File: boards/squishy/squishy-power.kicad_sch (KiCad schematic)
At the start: 48 parts, among them SW1 RST, U1 LFE5UM5G-45F-8BG381C, U10 TPS720115QDRVRQ1, U2 W25N01GVZEIG, U5 APX811-40UG-7, U7 TPS73733DRVR, U8 TPS7A1125PDRVT, U9 TPS7A1118PDRVT

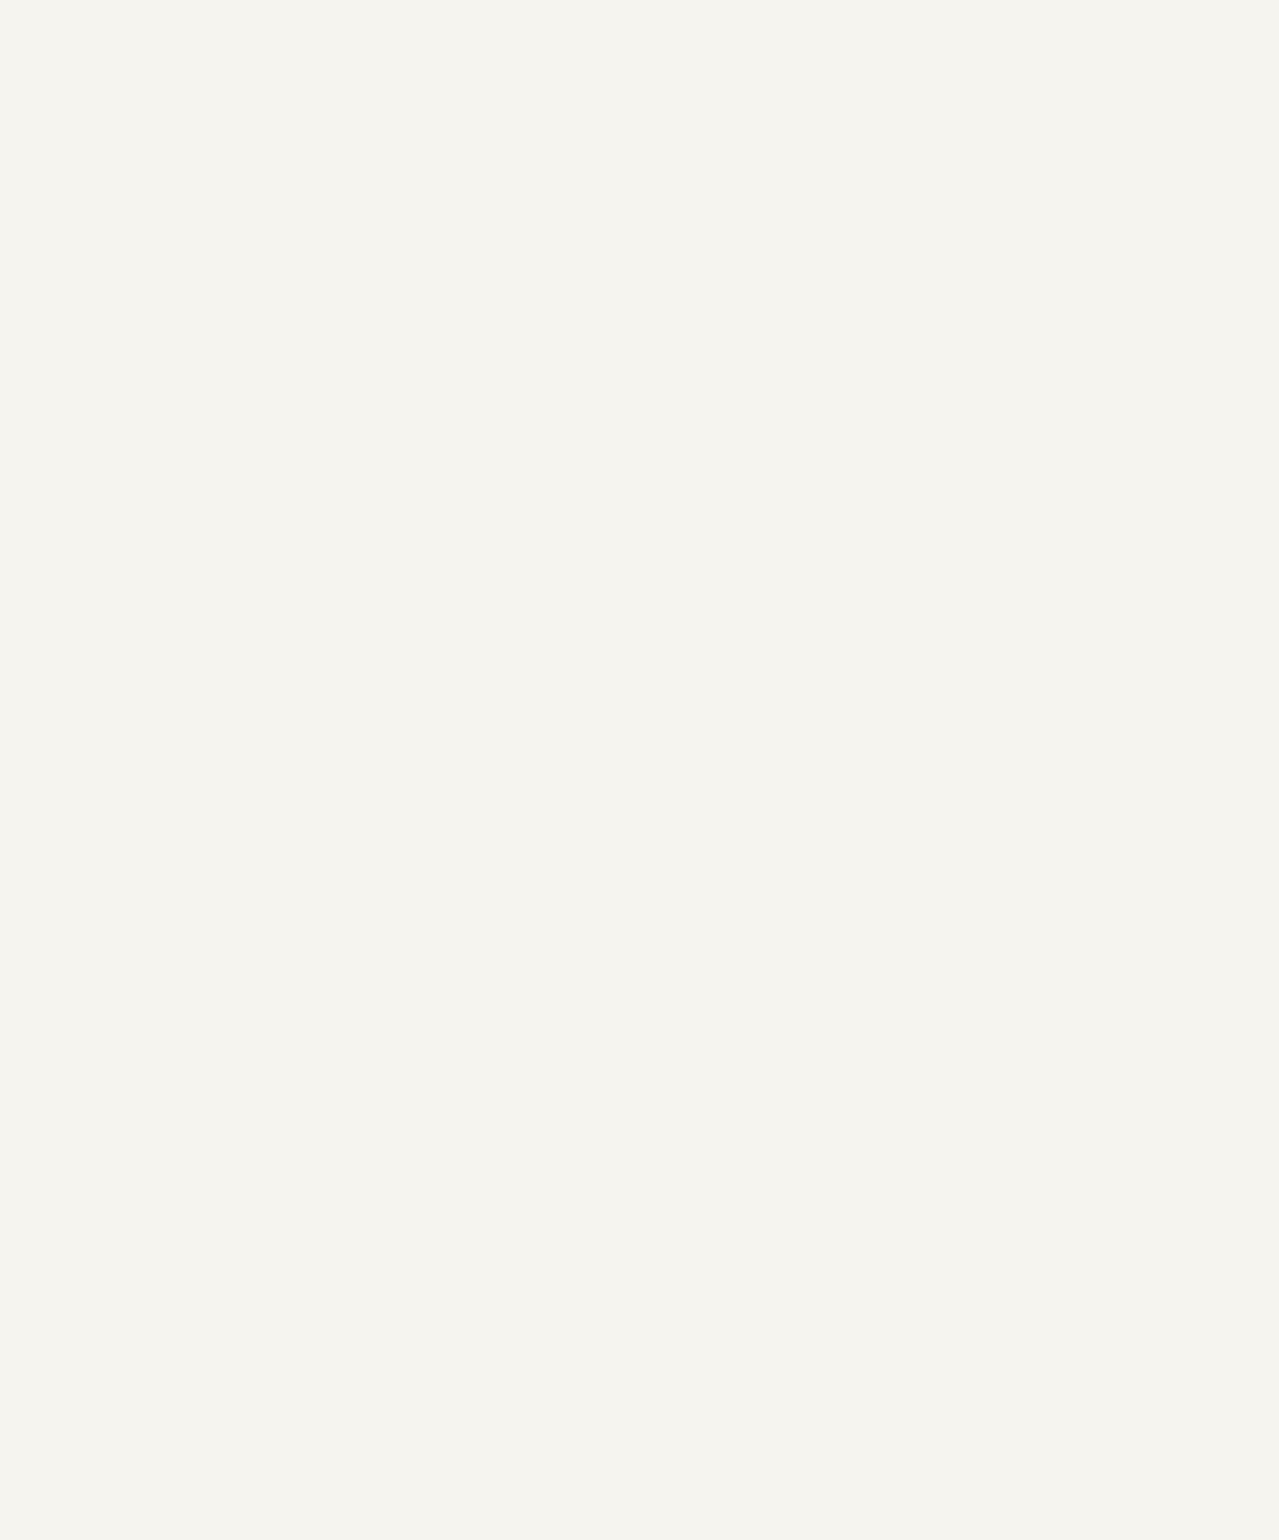
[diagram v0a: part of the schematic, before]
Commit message: hardware: large amount of refactoring and schematic tetris, slowly getting everything hooked back up, also merrged all the DFU/Debug signals onto a single connector
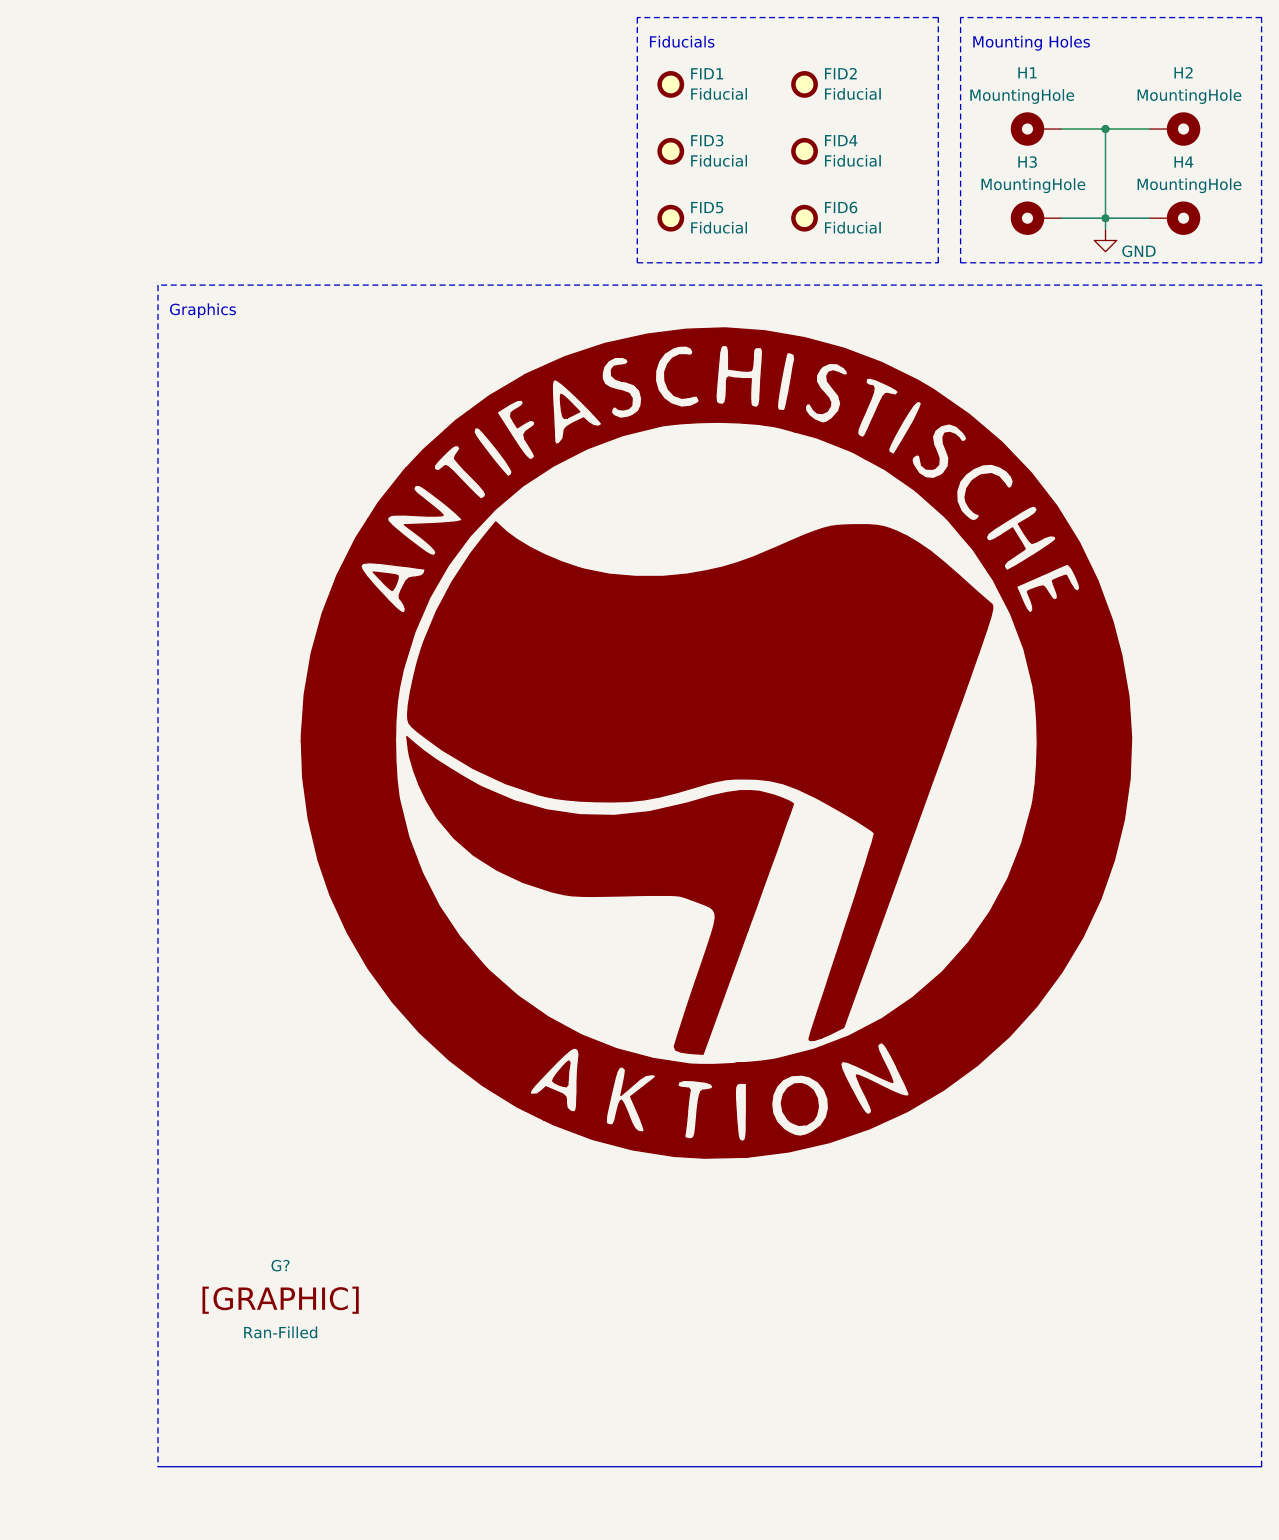
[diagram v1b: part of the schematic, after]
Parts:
- added FID1, FID2, FID3, FID4, FID5, FID6: Fiducial, Fiducial:Fiducial_0.75mm_Mask1.5mm, symbol Mechanical:Fiducial
- added G?: Ran-Filled, lethalbit-graphics:yuki_10x11, symbol lethalbit-graphics:Graphic
- added G?: Antifaschistische_Aktion, DX-MON:Antifaschistische-Aktion_Inv_600dpi, symbol lethalbit-graphics:Antifaschistische_Aktion
- added H1, H2, H3, H4: MountingHole, MountingHole:MountingHole_3.2mm_M3_Pad, symbol Mechanical:MountingHole_Pad
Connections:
- net GND: now also H1.1, H2.1, H3.1, H4.1
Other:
- note added: "Fiducials"
- note added: "Graphics"
- note added: "Mounting Holes"

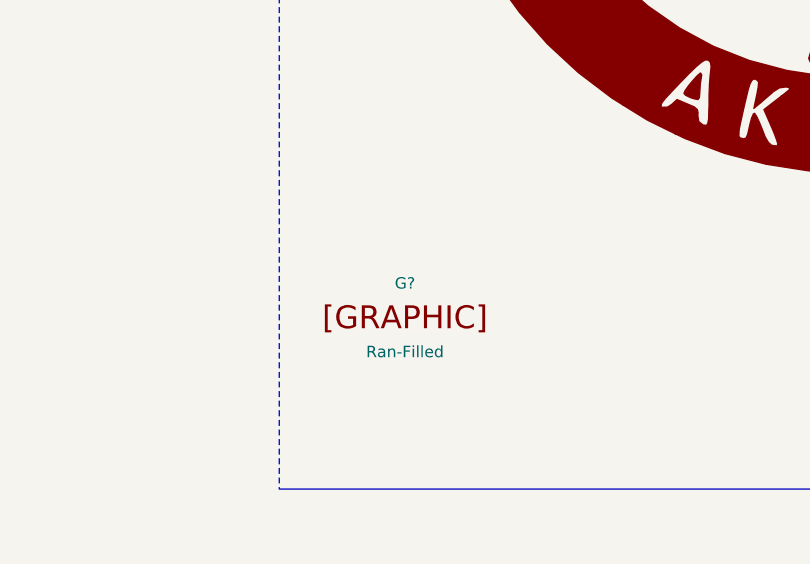
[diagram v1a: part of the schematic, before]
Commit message: hardware: some more refactoring, prior to a full PCB rip-up and re-layout
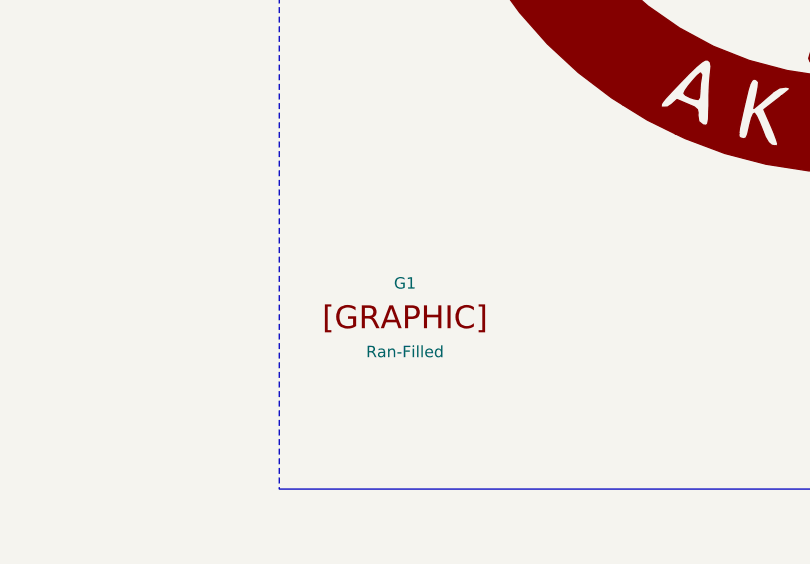
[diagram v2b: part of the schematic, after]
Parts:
- gave numbers to parts that had none: 2
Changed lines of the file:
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@@
   (symbol (lib_id "power:GND") (at 388.62 38.1 0) (unit 1)
     (in_bom yes) (on_board yes)
-    (property "Reference" "#PWR?" (id 0) (at 388.62 44.45 0)
+    (property "Reference" "#PWR0110" (id 0) (at 388.62 44.45 0)
       (effects (font (size 1.27 1.27)) hide)
     )
@@
   (symbol (lib_id "lethalbit-graphics:Graphic") (at 294.64 160.02 0) (unit 1)
     (in_bom no) (on_board yes)
-    (property "Reference" "G?" (id 0) (at 294.64 156.21 0))
+    (property "Reference" "G1" (id 0) (at 294.64 156.21 0))
     (property "Value" "Ran-Filled" (id 1) (at 294.64 163.83 0))
     (property "Footprint" "lethalbit-graphics:yuki_10x11" (id 2) (at 294.64 160.02 0)
@@
   (symbol (lib_id "lethalbit-graphics:Antifaschistische_Aktion") (at 344.17 46.99 0) (unit 1)
     (in_bom no) (on_board yes)
-    (property "Reference" "G?" (id 0) (at 392.2522 95.4532 0)
+    (property "Reference" "G2" (id 0) (at 392.2522 95.4532 0)
       (effects (font (size 1.27 1.27)) (justify left) hide)
     )

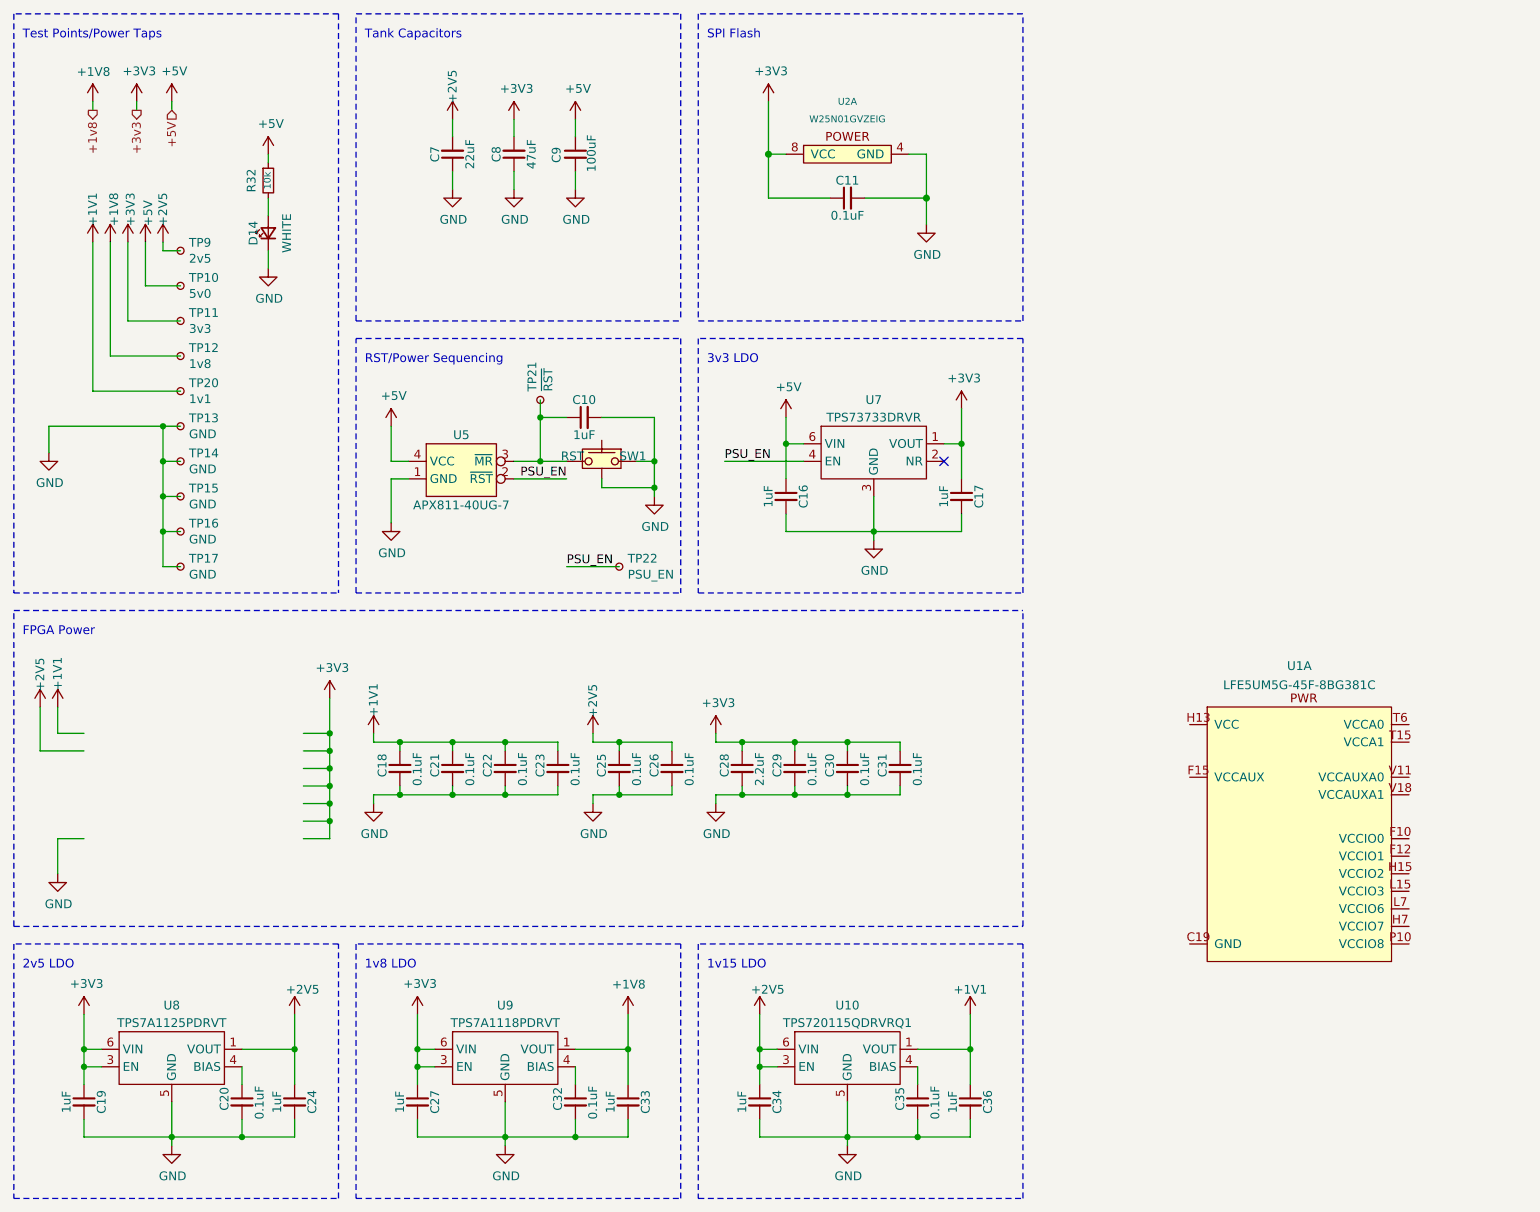
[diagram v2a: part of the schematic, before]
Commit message: hardware: added back the 1v8 regulated as we need the ULPI PHY again for USB2 compatibility, also updated the sheet metadata
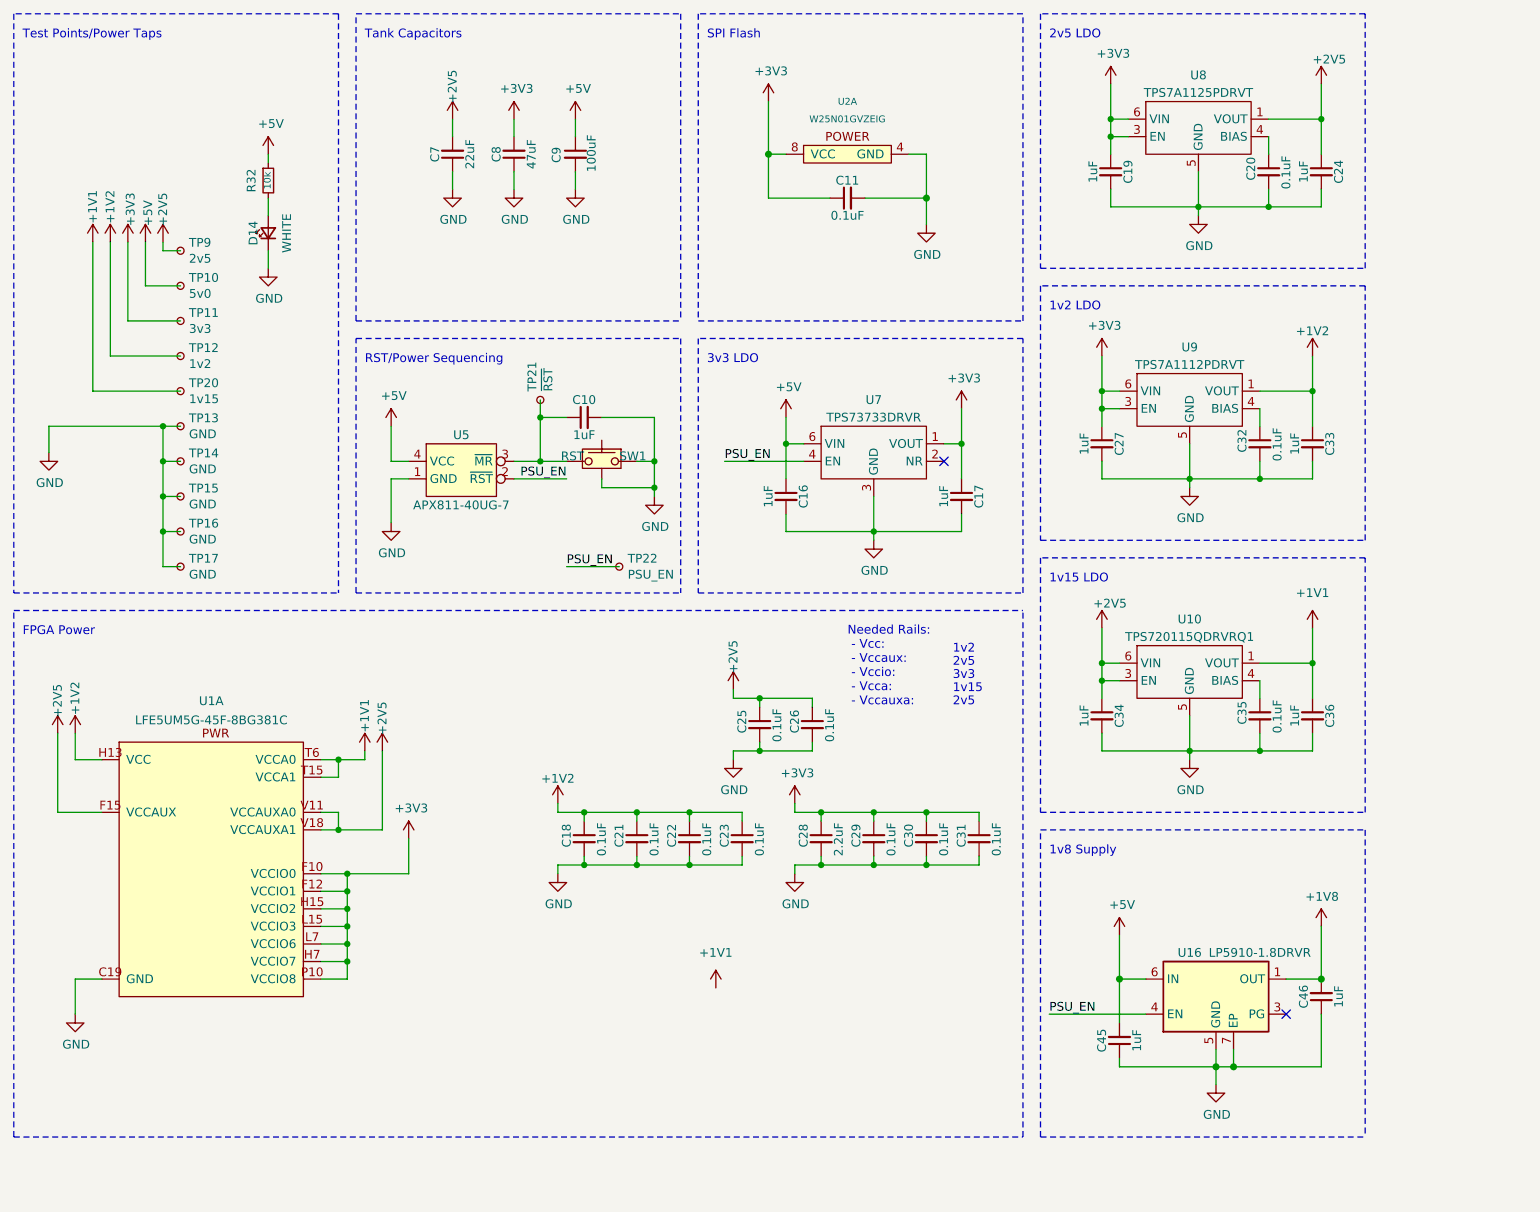
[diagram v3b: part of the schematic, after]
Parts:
- added C45, C46: 1uF, Capacitor_SMD:C_0603_1608Metric, symbol Device:C_Small
- added U16: LP5910-1.8DRVR, Package_SON:WSON-6-1EP_2x2mm_P0.65mm_EP1x1.6mm_ThermalVias, symbol Regulator_Linear:LP5912-1.8DRV
- TP12: value 1v8 -> 1v2
- TP20: value 1v1 -> 1v15
- U9: value TPS7A1118PDRVT -> TPS7A1112PDRVT; MPN TPS7A1118PDRVT -> TPS7A1112PDRVT
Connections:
- net +1V1: now also U1.T15 (VCCA1), U1.T6 (VCCA0), U1.U15 (VCCA1), U1.U6 (VCCA0); no longer C18.1, C21.1, C22.1, C23.1
- net +1V8: now also C46.2, U16.1 (OUT); no longer C33.1, TP12.1, U9.1 (VOUT), U9.2 (NC)
- net +2V5: now also U1.F15 (VCCAUX), U1.F6 (VCCAUX), U1.P15 (VCCAUX), U1.P6 (VCCAUX), U1.V10 (VCCAUXA0), U1.V11 (VCCAUXA0), U1.V17 (VCCAUXA1), U1.V18 (VCCAUXA1)
- net +3V3: now also U1.F10 (VCCIO0), U1.F11 (VCCIO1), U1.F12 (VCCIO1), U1.F9 (VCCIO0), U1.H14 (VCCIO2), U1.H15 (VCCIO2), U1.H6 (VCCIO7), U1.H7 (VCCIO7), U1.J15 (VCCIO2), U1.J6 (VCCIO7), U1.L14 (VCCIO3), U1.L15 (VCCIO3), U1.L6 (VCCIO6), U1.L7 (VCCIO6), U1.M15 (VCCIO3), U1.M6 (VCCIO6), U1.P10 (VCCIO8), U1.P9 (VCCIO8)
- net +5V: now also C45.2, U16.6 (IN)
- net GND: now also U1.B14 (GND), U1.B7 (GND), U1.C19 (GND), U1.D4 (GND), U1.F13 (GND), U1.F14 (GND), U1.F7 (GND), U1.F8 (GND), U1.G10 (GND), U1.G11 (GND), U1.G12 (GND), U1.G13 (GND), U1.G14 (GND), U1.G15 (GND), U1.G17 (GND), U1.G4 (GND), U1.G6 (GND), U1.G7 (GND), U1.G8 (GND), U1.G9 (GND), U1.H19 (GND), U1.J10 (GND), U1.J11 (GND), U1.J12 (GND), U1.J14 (GND), U1.J2 (GND), U1.J7 (GND), U1.J9 (GND), U1.K10 (GND), U1.K11 (GND), U1.K12 (GND), U1.K14 (GND), U1.K15 (GND), U1.K6 (GND), U1.K7 (GND), U1.K9 (GND), U1.L10 (GND), U1.L11 (GND), U1.L12 (GND), U1.L9 (GND), U1.M10 (GND), U1.M11 (GND), U1.M12 (GND), U1.M14 (GND), U1.M16 (GND), U1.M2 (GND), U1.M7 (GND), U1.M9 (GND), U1.N14 (GND), U1.N15 (GND), U1.N6 (GND), U1.N7 (GND), U1.P11 (GND), U1.P12 (GND), U1.P13 (GND), U1.P14 (GND), U1.P7 (GND), U1.P8 (GND), U1.R19 (GND), U1.U10 (GND), U1.U11 (GND), U1.U12 (GND), U1.U13 (GND), U1.U14 (GND), U1.U7 (GND), U1.U8 (GND), U1.U9 (GND), U1.V12 (GND), U1.V13 (GND), U1.V14 (GND), U1.V15 (GND), U1.V16 (GND), U1.V19 (GND), U1.V20 (GND), U1.V5 (GND), U1.V6 (GND), U1.V7 (GND), U1.V8 (GND), U1.V9 (GND), U1.W12 (GND), U1.W15 (GND), U1.W16 (GND), U1.W19 (GND), U1.W6 (GND), U1.W7 (GND), C45.1, C46.1, U16.5 (GND), U16.7 (EP)
- net PSU_EN: now also U16.4 (EN)
- net +1V2: now reaches U1.H10 (VCC), U1.H11 (VCC), U1.H12 (VCC), U1.H13 (VCC), U1.H8 (VCC), U1.H9 (VCC), U1.J13 (VCC), U1.J8 (VCC), U1.K13 (VCC), U1.K8 (VCC), U1.L13 (VCC), U1.L8 (VCC), U1.M13 (VCC), U1.M8 (VCC), U1.N10 (VCC), U1.N11 (VCC), U1.N12 (VCC), U1.N13 (VCC), U1.N8 (VCC), U1.N9 (VCC)
- net +1V2: now also C18.1, C21.1, C22.1, C23.1, C33.1, TP12.1, U9.1 (VOUT), U9.2 (NC)
- no-connect marks 1 -> 2
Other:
- note added: "1v15"
- note added: "1v2"
- note added: "1v2 LDO"
- note added: "1v8 Supply"
- note added: "2v5"
- note added: "3v3"
- note added: "Needed Rails: - Vcc: - Vccaux: - Vccio: - Vcca: - Vccauxa:"
- note removed: "1v8 LDO"
- moved on the sheet: C18, C19, C20, C21, C22, C23, C24, C25, C26, C27, C28, C29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
